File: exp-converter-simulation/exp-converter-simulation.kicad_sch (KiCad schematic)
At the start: 9 parts, among them Q1 BC547, Q2 BC547, U1 TL071

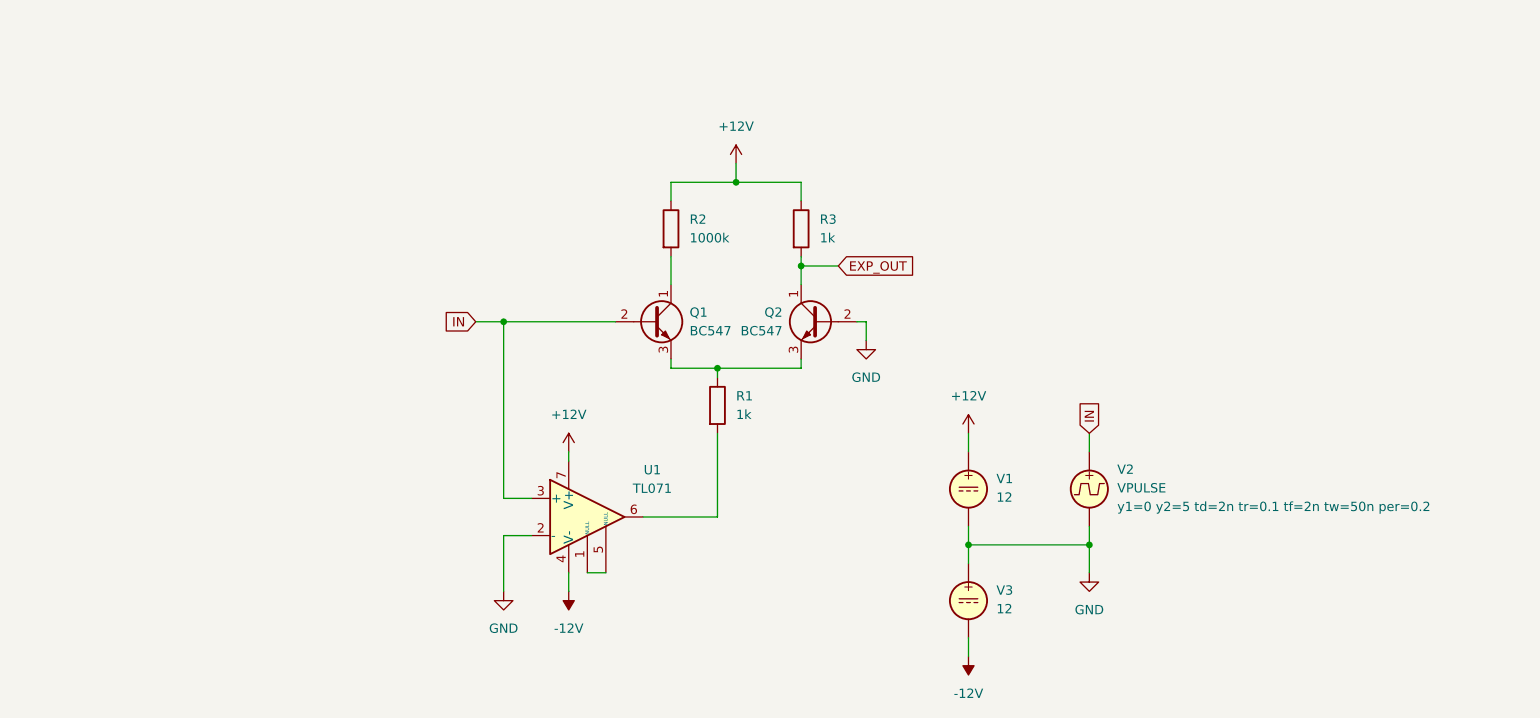
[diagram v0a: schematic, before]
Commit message: Exp converter simmulation works
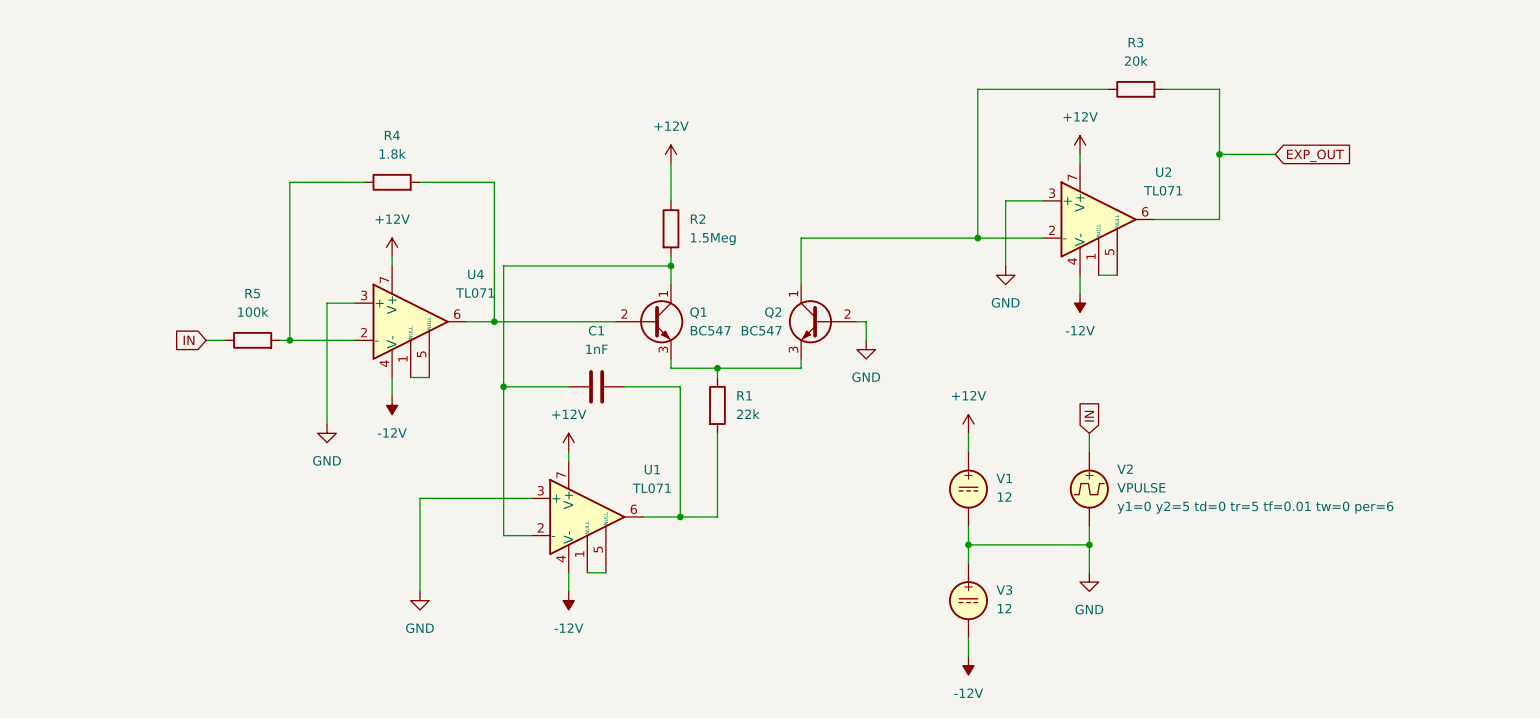
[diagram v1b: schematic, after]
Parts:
- added C1: 1nF, symbol Device:C
- added R4: 1.8k, symbol Device:R
- added R5: 100k, symbol Device:R
- added U2, U4: TL071, symbol Amplifier_Operational:TL071
- R1: value 1k -> 22k
- R2: value 1000k -> 1.5Meg
- R3: value 1k -> 20k
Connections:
- net +12V: now also U2.7 (V+), U4.7 (V+); no longer R3.1
- net -12V: now also U2.4 (V-), U4.4 (V-)
- net EXP_OUT: now also U2.6; no longer Q2.1 (C)
- net GND: now also U1.3 (+), U2.3 (+), U4.3 (+); no longer U1.2 (-)
- net IN: now also R5.1; no longer Q1.2 (B), U1.3 (+)
- net at Q1.1 (C), R2.2: now also U1.2 (-), C1.1
- net at R1.2, U1.6: now also C1.2
- new net: R4.1, R5.2, U4.2 (-)
- new net: Q1.2 (B), R4.2, U4.6
- new net: Q2.1 (C), R3.1, U2.2 (-)
- new net: U2.1 (NULL), U2.5 (NULL)
- new net: U4.1 (NULL), U4.5 (NULL)

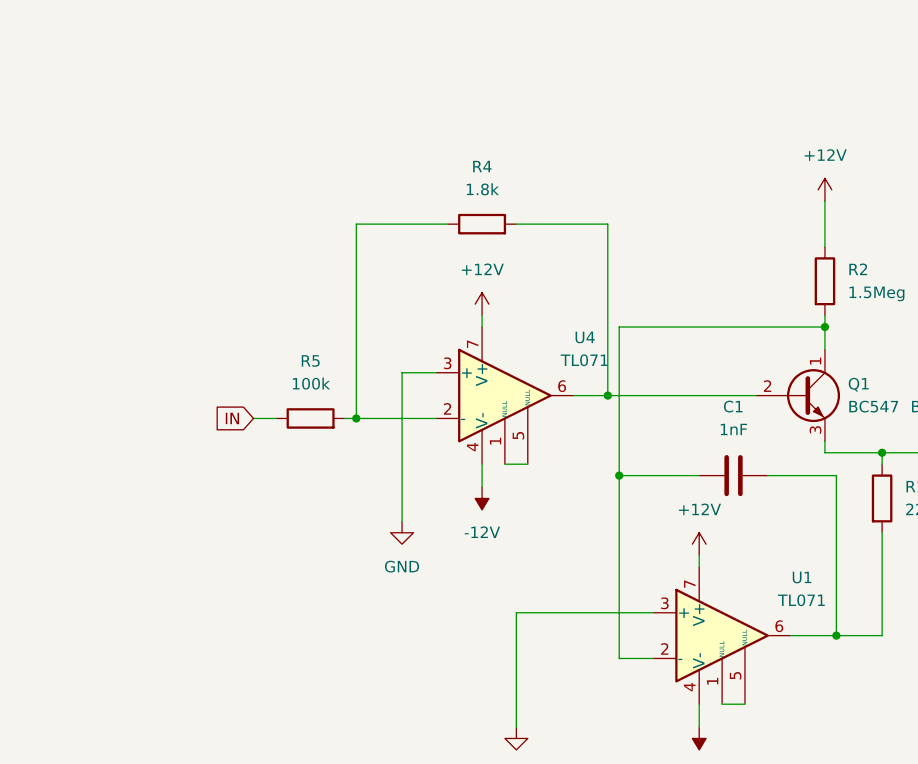
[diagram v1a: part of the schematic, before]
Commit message: Fix potentiometers footprint.
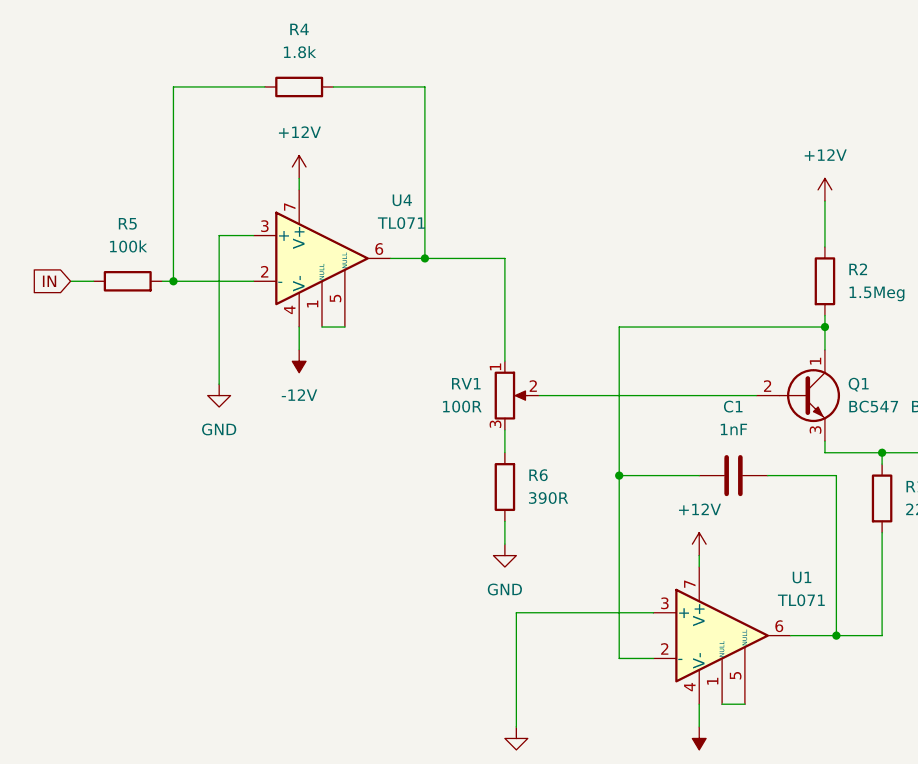
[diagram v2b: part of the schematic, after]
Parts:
- added R6: 390R, symbol Device:R
- added RV1: 100R, symbol Device:R_Potentiometer
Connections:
- net GND: now also R6.1
- net at R4.2, U4.6: now also RV1.1; no longer Q1.2 (B)
- new net: Q1.2 (B), RV1.2
- new net: R6.2, RV1.3
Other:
- moved on the sheet: R4, R5, U4
